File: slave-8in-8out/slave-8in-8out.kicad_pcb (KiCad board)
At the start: 2 copper layers, 69.6 x 71.6 mm, 87 parts, among them J1 Conn_01x06_Male, J2 Screw_Terminal_01x02, J3 Conn_01x06_Female, J4 Screw_Terminal_01x04, J5 Screw_Terminal_01x04, J6 Screw_Terminal_01x04, J7 Screw_Terminal_01x04, J8 Conn_01x10_Female, J9 Screw_Terminal_01x02, SW1 SW_DIP_x03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

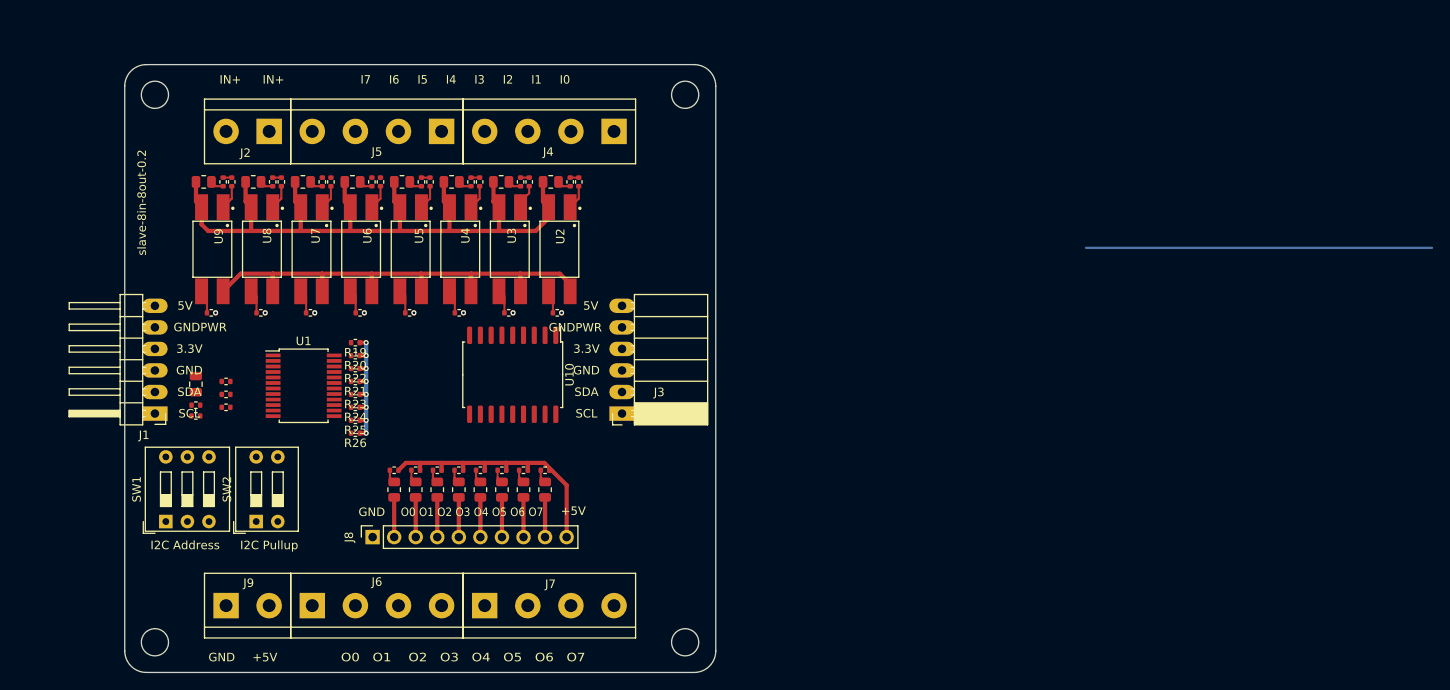
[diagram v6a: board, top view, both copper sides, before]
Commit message: update slave-8in-8out routing
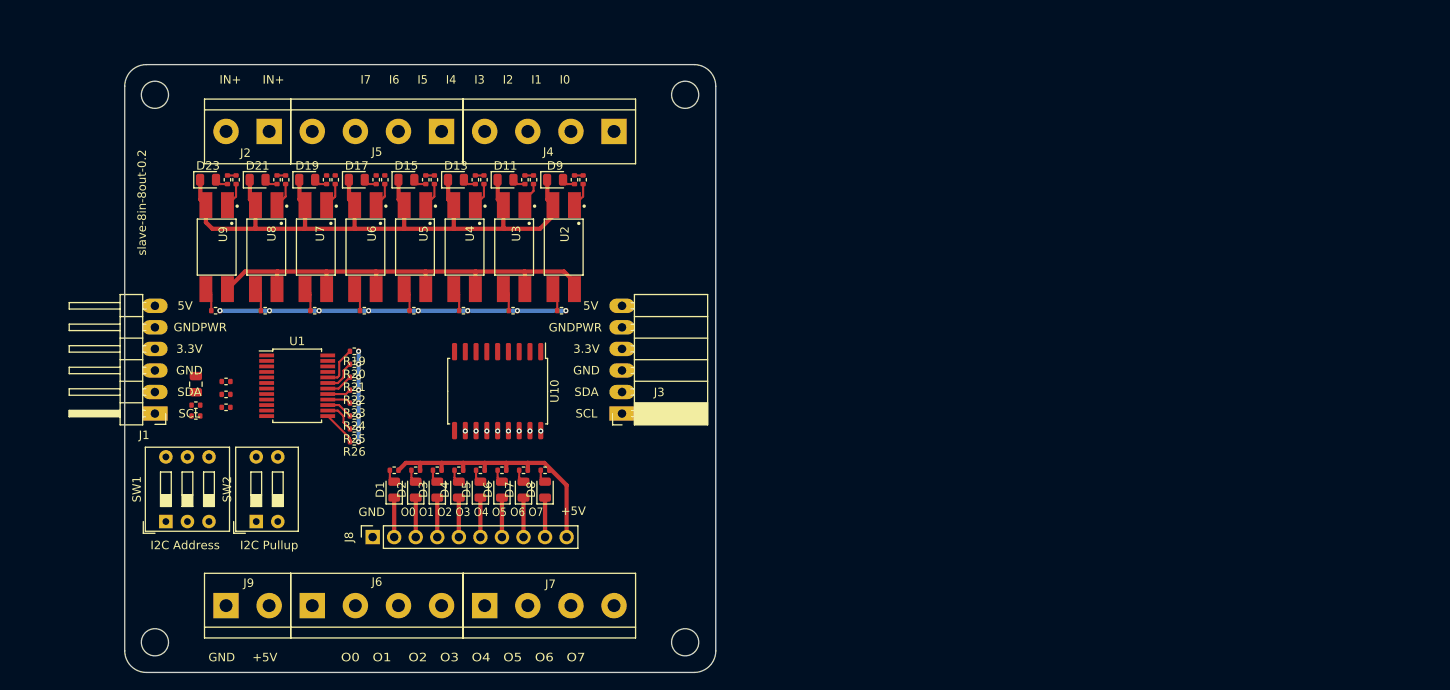
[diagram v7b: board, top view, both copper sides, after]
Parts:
- D1, D11, D13, D15, D17, D19, D2, D21, D23, D3, D4, D5, D6, D7, D8, D9: footprint Resistor_SMD:R_0805_2012Metric -> LED_SMD:LED_0805_2012Metric
- U2, U3, U4, U5, U6, U7, U8, U9: value EL817S1(C)(TU)-F -> EL817
- moved U10 2.62 mm to (113.5, 98.7)
- moved R22 2.54 mm to (96.6, 98.6)
- moved R19 1.02 mm to (96.6, 94.0)
- moved R20 1.02 mm to (96.6, 95.5)
- moved R23 1.02 mm to (96.6, 100.1)
- moved R24 1.02 mm to (96.6, 101.6)
- moved R25 1.02 mm to (96.6, 103.1)
- moved R26 1.02 mm to (96.6, 104.6)
- moved U1 0.76 mm to (89.9, 98.0)
- moved D13 0.57 mm to (108.6, 73.8)
- moved D15 0.57 mm to (102.8, 73.8)
- moved D17 0.57 mm to (96.9, 73.8)
- moved D19 0.57 mm to (91.1, 73.8)
- moved R32 0.57 mm to (105.1, 73.8)
- moved R35 0.57 mm to (99.2, 73.8)
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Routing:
- net +3V3: track 72.4 -> 66.3 mm
- net GPA7: track 0.00 -> 4.83 mm
- net GPA0: track 0.00 -> 4.11 mm
- net GPA6: track 0.00 -> 4.00 mm
- net GPA1: track 0.00 -> 3.94 mm
- net GPA5: track 0.00 -> 3.18 mm
- net GPA2: track 0.00 -> 3.15 mm
- net GPA4: track 0.00 -> 2.81 mm
- net GPA3: track 0.00 -> 2.79 mm
- net O7: track 4.68 -> 4.72 mm, vias 0 -> 1
- net O6: track 4.68 -> 4.72 mm, vias 0 -> 1
- net O5: track 4.68 -> 4.72 mm, vias 0 -> 1
- net O4: track 4.68 -> 4.72 mm, vias 0 -> 1
- net O3: track 4.68 -> 4.72 mm, vias 0 -> 1
- net O2: track 4.68 -> 4.72 mm, vias 0 -> 1
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
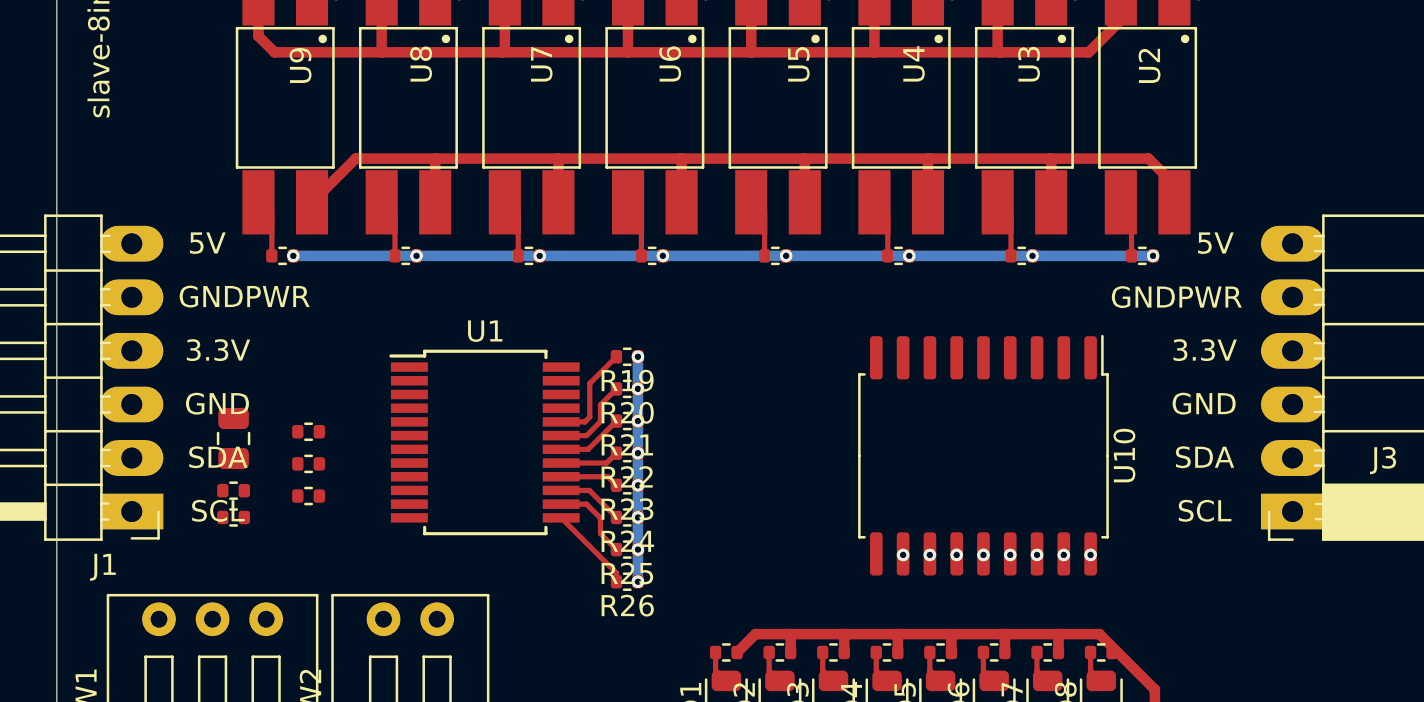
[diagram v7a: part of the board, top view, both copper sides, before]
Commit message: update slave-8in-8out routing
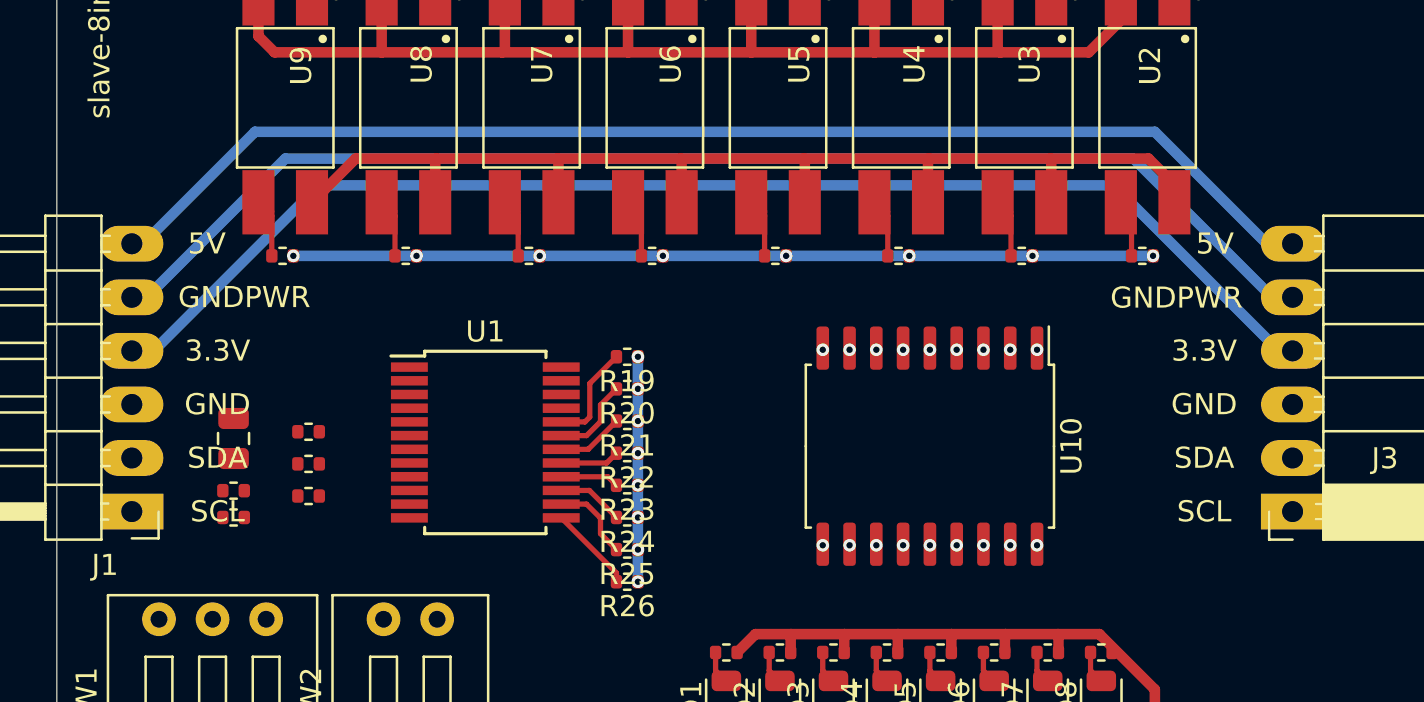
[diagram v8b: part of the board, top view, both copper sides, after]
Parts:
- moved U10 2.58 mm to (111.0, 98.2)
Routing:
- net +3V3: track 66.3 -> 127.9 mm
- net GNDPWR: track 88.1 -> 148.6 mm
- net +5V: track 32.6 -> 92.1 mm, vias 0 -> 1
- net GPA7: track 4.83 -> 4.91 mm, vias 0 -> 1
- net GPA6: track 4.00 -> 4.08 mm, vias 0 -> 1
- net GPA5: track 3.18 -> 3.25 mm, vias 0 -> 1
- net GPA4: track 2.81 -> 2.89 mm, vias 0 -> 1
- net GPA3: track 2.79 -> 2.87 mm, vias 0 -> 1
- net GPA2: track 3.15 -> 3.23 mm, vias 0 -> 1
- net GPA1: track 3.94 -> 4.02 mm, vias 0 -> 1
- net GPA0: track 4.11 -> 4.19 mm, vias 0 -> 1
- net GND: vias 8 -> 9
